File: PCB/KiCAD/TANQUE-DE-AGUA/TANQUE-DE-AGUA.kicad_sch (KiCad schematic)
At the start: 39 parts, among them J2 Vca_OUT, J5 HX30002-BA, Q1 2N3904, SW1 Nivel MAX, SW2 Nivel Min, U1 74HC00, U2 ULN2003, U3 LM7805, U4 74HC14, U5 MOC3021M, U6 BTA16-600C

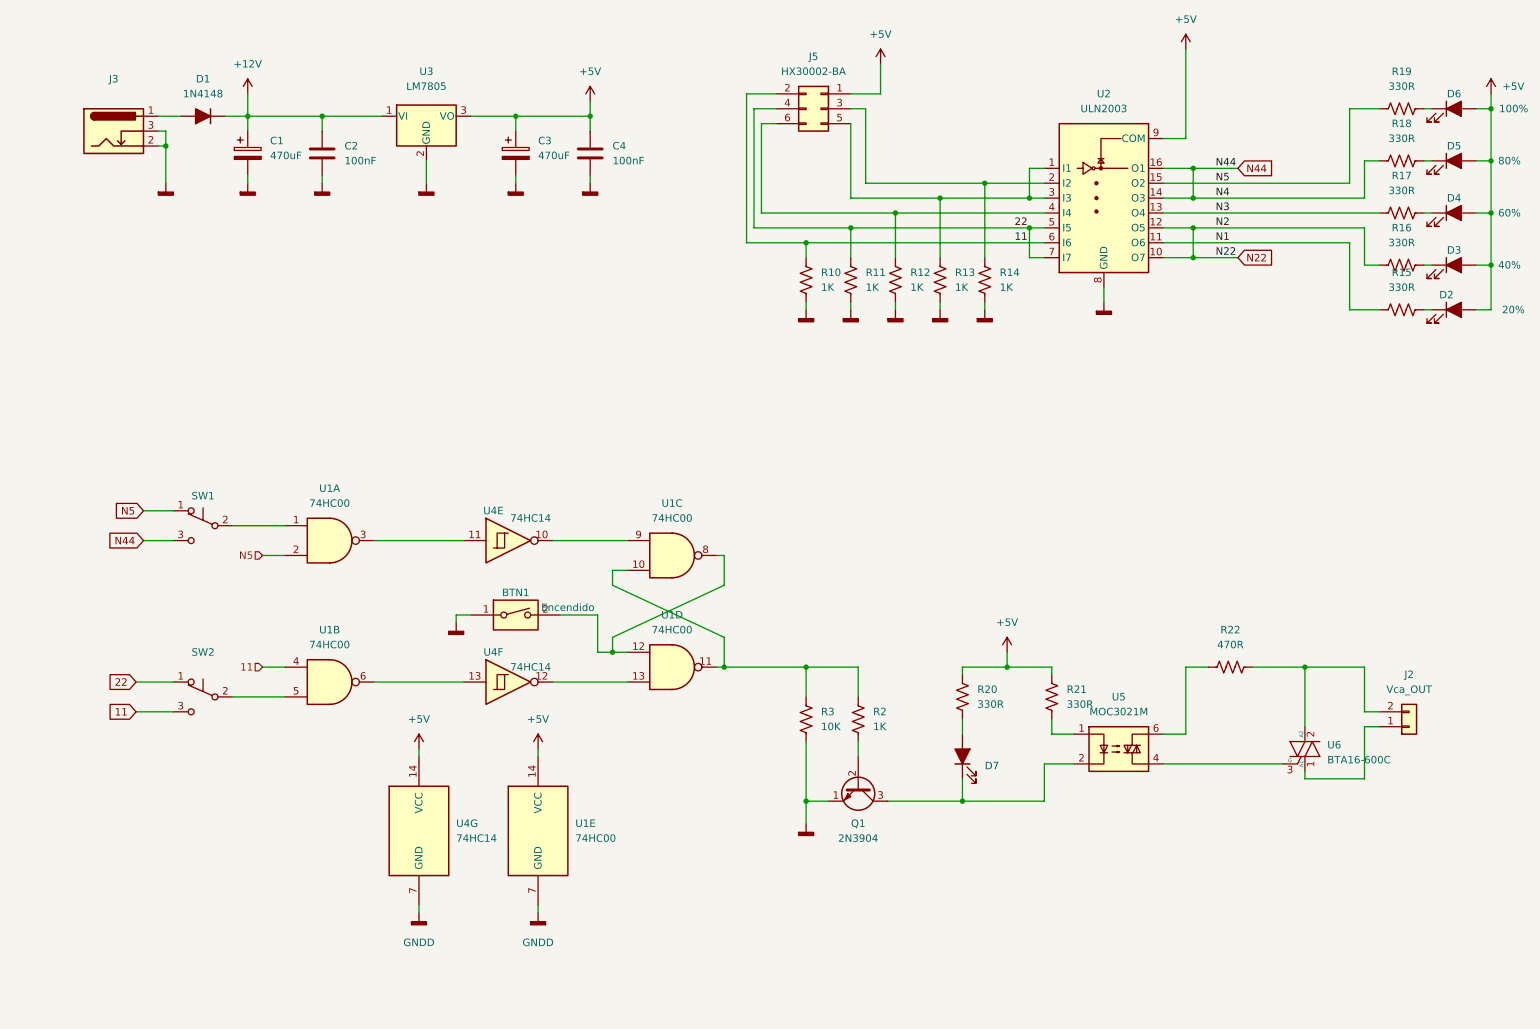
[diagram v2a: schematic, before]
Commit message: actualizacion del esquematico en Proteus y en KiCAD
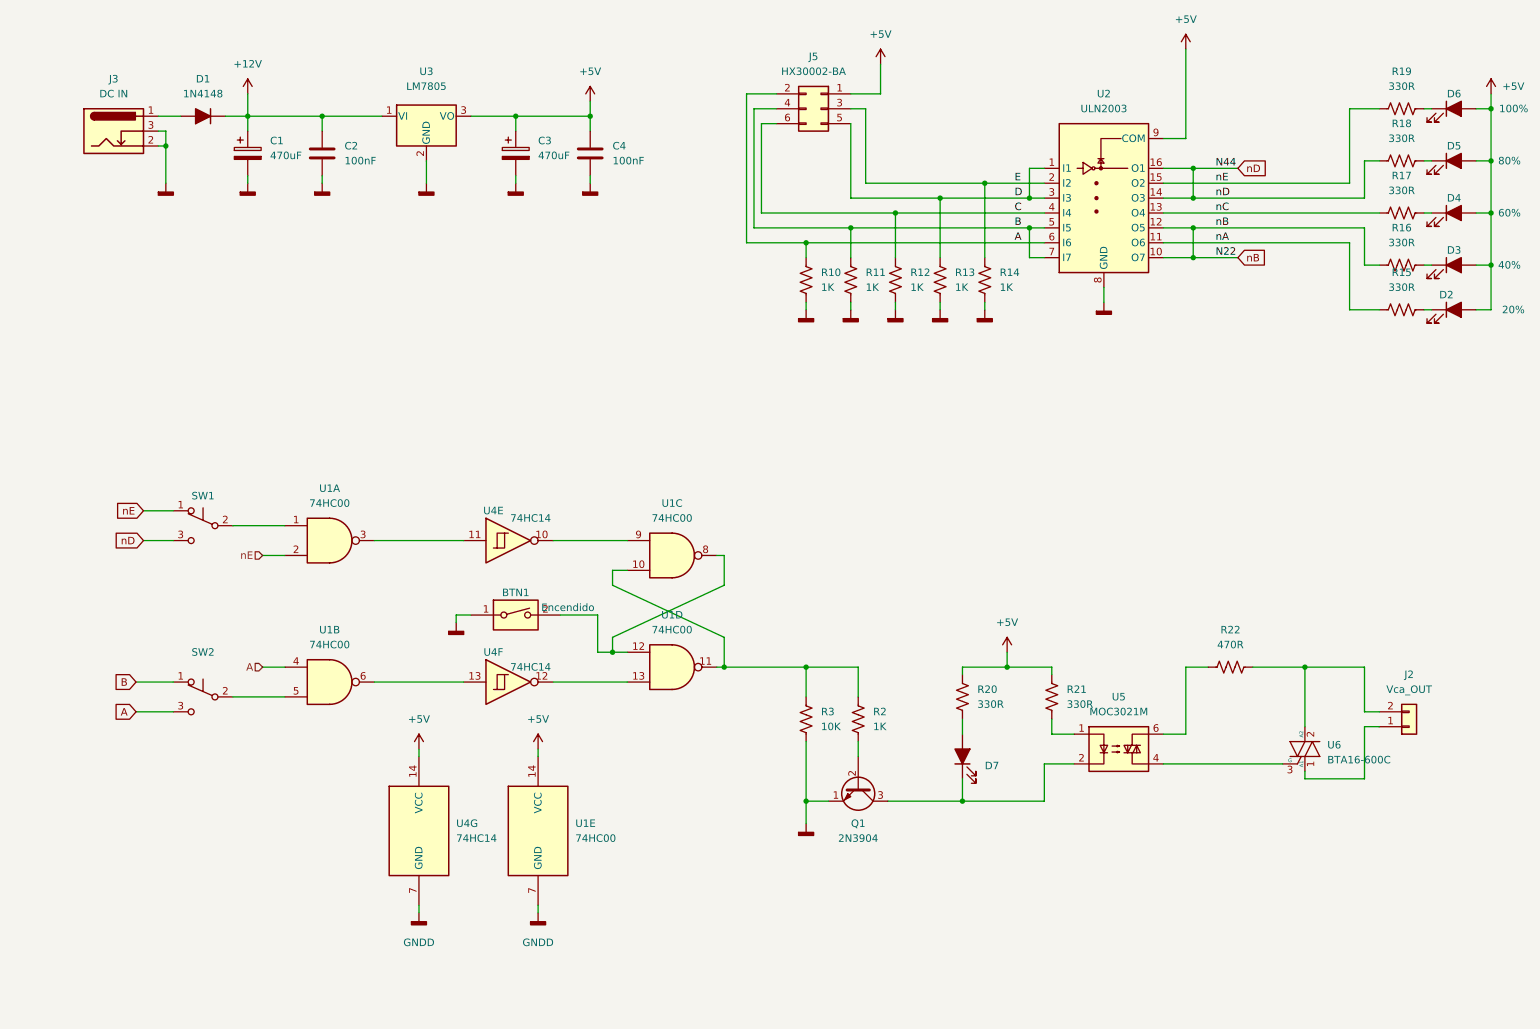
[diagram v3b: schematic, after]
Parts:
- J3: value (none) -> DC IN; footprint (none) -> Connector_BarrelJack:BarrelJack_Horizontal
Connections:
- net C: now reaches J5.6 (Pin_6), R12.1, U2.4 (I4)
- net E: now reaches J5.3 (Pin_3), R14.1, U2.2 (I2)
- net D: now reaches J5.5 (Pin_5), R13.1, U2.1 (I1), U2.3 (I3)
- net 11 renamed A
- net 22 renamed B
- net N1 renamed nA
- net N22 renamed nB
- net N3 renamed nC
- net N44 renamed nD
- net N5 renamed nE
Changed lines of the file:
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@@
     (stroke (width 0) (type default) (color 0 0 0 0))
   )
-  (label "N3" (at 220.98 50.8 0)
-    (effects (font (size 1.27 1.27)) (justify left bottom))
-  )
-  (label "N4" (at 220.98 48.26 0)
-    (effects (font (size 1.27 1.27)) (justify left bottom))
-  )
-  (label "N2" (at 220.98 53.34 0)
-    (effects (font (size 1.27 1.27)) (justify left bottom))
-  )
-  (label "N1" (at 220.98 55.88 0)
-    (effects (font (size 1.27 1.27)) (justify left bottom))
-  )
-  (label "N5" (at 220.98 45.72 0)
-    (effects (font (size 1.27 1.27)) (justify left bottom))
-  )
-  (label "11" (at 186.69 55.88 0)
+  (label "E" (at 186.69 45.72 0)
+    (effects (font (size 1.27 1.27)) (justify left bottom))
+  )
+  (label "nC" (at 220.98 50.8 0)
+    (effects (font (size 1.27 1.27)) (justify left bottom))
+  )
+  (label "nD" (at 220.98 48.26 0)
+    (effects (font (size 1.27 1.27)) (justify left bottom))
+  )
+  (label "nB" (at 220.98 53.34 0)
+    (effects (font (size 1.27 1.27)) (justify left bottom))
+  )
+  (label "D" (at 186.69 48.26 0)
+    (effects (font (size 1.27 1.27)) (justify left bottom))
+  )
+  (label "nA" (at 220.98 55.88 0)
+    (effects (font (size 1.27 1.27)) (justify left bottom))
+  )
+  (label "nE" (at 220.98 45.72 0)
+    (effects (font (size 1.27 1.27)) (justify left bottom))
+  )
+  (label "A" (at 186.69 55.88 0)
+    (effects (font (size 1.27 1.27)) (justify left bottom))
+  )
+  (label "C" (at 186.69 50.8 0)
     (effects (font (size 1.27 1.27)) (justify left bottom))
   )
@@
     (effects (font (size 1.27 1.27)) (justify left bottom))
   )
-  (label "22" (at 186.69 53.34 0)
-    (effects (font (size 1.27 1.27)) (justify left bottom))
-  )
-  (global_label "N22" (shape input) (at 224.79 58.42 0) (fields_autoplaced)
+  (label "B" (at 186.69 53.34 0)
+    (effects (font (size 1.27 1.27)) (justify left bottom))
+  )
+  (global_label "nB" (shape input) (at 224.79 58.42 0) (fields_autoplaced)
     (effects (font (size 1.27 1.27)) (justify left))
-    (property "Referencias entre hojas" "${INTERSHEET_REFS}" (id 0) (at 230.9526 58.3406 0)
+    (property "Referencias entre hojas" "${INTERSHEET_REFS}" (id 0) (at 229.6221 58.3406 0)
       (effects (font (size 1.27 1.27)) (justify left) hide)
     )
   )
-  (global_label "N44" (shape input) (at 38.1 106.68 180) (fields_autoplaced)
+  (global_label "nD" (shape input) (at 38.1 106.68 180) (fields_autoplaced)
     (effects (font (size 1.27 1.27)) (justify right))
-    (property "Referencias entre hojas" "${INTERSHEET_REFS}" (id 0) (at 31.9374 106.6006 0)
+    (property "Referencias entre hojas" "${INTERSHEET_REFS}" (id 0) (at 33.2679 106.6006 0)
       (effects (font (size 1.27 1.27)) (justify right) hide)
     )
   )
-  (global_label "N44" (shape input) (at 224.79 43.18 0) (fields_autoplaced)
+  (global_label "nD" (shape input) (at 224.79 43.18 0) (fields_autoplaced)
     (effects (font (size 1.27 1.27)) (justify left))
-    (property "Referencias entre hojas" "${INTERSHEET_REFS}" (id 0) (at 230.9526 43.1006 0)
+    (property "Referencias entre hojas" "${INTERSHEET_REFS}" (id 0) (at 229.6221 43.1006 0)
       (effects (font (size 1.27 1.27)) (justify left) hide)
     )
   )
-  (global_label "N5" (shape input) (at 38.1 101.6 180) (fields_autoplaced)
+  (global_label "nE" (shape input) (at 38.1 101.6 180) (fields_autoplaced)
     (effects (font (size 1.27 1.27)) (justify right))
-    (property "Referencias entre hojas" "${INTERSHEET_REFS}" (id 0) (at 33.1469 101.5206 0)
+    (property "Referencias entre hojas" "${INTERSHEET_REFS}" (id 0) (at 33.3888 101.5206 0)
       (effects (font (size 1.27 1.27)) (justify right) hide)
     )
   )
-  (global_label "22" (shape input) (at 36.83 130.81 180) (fields_autoplaced)
+  (global_label "B" (shape input) (at 36.83 130.81 180) (fields_autoplaced)
     (effects (font (size 1.27 1.27)) (justify right))
-    (property "Referencias entre hojas" "${INTERSHEET_REFS}" (id 0) (at 31.9979 130.7306 0)
+    (property "Referencias entre hojas" "${INTERSHEET_REFS}" (id 0) (at 33.1469 130.7306 0)
       (effects (font (size 1.27 1.27)) (justify right) hide)
     )
   )
-  (global_label "11" (shape input) (at 36.83 135.89 180) (fields_autoplaced)
+  (global_label "A" (shape input) (at 36.83 135.89 180) (fields_autoplaced)
     (effects (font (size 1.27 1.27)) (justify right))
-    (property "Referencias entre hojas" "${INTERSHEET_REFS}" (id 0) (at 31.9979 135.8106 0)
+    (property "Referencias entre hojas" "${INTERSHEET_REFS}" (id 0) (at 33.3283 135.8106 0)
       (effects (font (size 1.27 1.27)) (justify right) hide)
     )
   )
-  (hierarchical_label "11" (shape input) (at 58.42 128.27 180)
+  (hierarchical_label "A" (shape input) (at 58.42 128.27 180)
     (effects (font (size 1.27 1.27)) (justify right))
   )
-  (hierarchical_label "N5" (shape input) (at 58.42 109.22 180)
+  (hierarchical_label "nE" (shape input) (at 58.42 109.22 180)
     (effects (font (size 1.27 1.27)) (justify right))
   )
@@
     (in_bom yes) (on_board yes) (fields_autoplaced)
     (property "Reference" "J3" (id 0) (at 33.02 27.94 0))
-    (property "Value" "" (id 1) (at 33.02 30.48 0))
-    (property "Footprint" "" (id 2) (at 34.29 37.846 0)
-      (effects (font (size 1.27 1.27)) hide)
-    )
+    (property "Value" "DC IN" (id 1) (at 33.02 30.48 0))
+    (property "Footprint" "Connector_BarrelJack:BarrelJack_Horizontal" (id 2) (at 34.29 37.846 0)
+      (effects (font (size 1.27 1.27)) hide)
+    )

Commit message: actualizacion del PCB
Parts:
- added H1, H2, H3, H4: MountingHole, MountingHole:MountingHole_2.7mm_M2.5, symbol Mechanical:MountingHole
- C1, C3: footprint Capacitor_THT:CP_Radial_D6.3mm_P2.50mm -> (none)
- Q1: footprint Package_TO_SOT_THT:TO-92_Inline -> Package_TO_SOT_THT:TO-92_Wide
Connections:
- net nE: now also U1.1; no longer U1.2
- net at SW1.2 (B): now also U1.2; no longer U1.1
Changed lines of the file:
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@@
     (pin "2")
   )
-  (symbol (lib_id "74xx:74HC00") (at 69.85 106.68 0) (unit 1)
+  (symbol (lib_id "74xx:74HC00") (at 69.85 106.68 0) (mirror x) (unit 1)
     (in_bom yes) (on_board yes) (fields_autoplaced)
     (property "Reference" "U1" (id 0) (at 69.85 97.79 0))
@@
       (effects (font (size 1.27 1.27)) (justify left))
     )
-    (property "Footprint" "Capacitor_THT:CP_Radial_D6.3mm_P2.50mm" (id 2) (at 102.5652 44.45 0)
+    (property "Footprint" "" (id 2) (at 102.5652 44.45 0)
       (effects (font (size 1.27 1.27)) hide)
     )
@@
     (property "Reference" "Q1" (id 0) (at 160.02 154.94 90))
     (property "Value" "2N3904" (id 1) (at 160.02 157.48 90))
-    (property "Footprint" "Package_TO_SOT_THT:TO-92_Inline" (id 2) (at 158.115 153.67 0)
+    (property "Footprint" "Package_TO_SOT_THT:TO-92_Wide" (id 2) (at 158.115 153.67 0)
       (effects (font (size 1.27 1.27) italic) (justify left) hide)
     )
@@
     (pin "3")
   )
+  (symbol (lib_id "Mechanical:MountingHole") (at 247.65 88.9 0) (unit 1)
+    (in_bom yes) (on_board yes) (fields_autoplaced)
+    (property "Reference" "H1" (id 0) (at 250.19 87.6299 0)
+      (effects (font (size 1.27 1.27)) (justify left) hide)
+    )
+    (property "Value" "MountingHole" (id 1) (at 250.19 88.8999 0)
+      (effects (font (size 1.27 1.27)) (justify left) hide)
+    )
+    (property "Footprint" "MountingHole:MountingHole_2.7mm_M2.5" (id 2) (at 247.65 88.9 0)
+      (effects (font (size 1.27 1.27)) hide)
+    )
+    (property "Datasheet" "~" (id 3) (at 247.65 88.9 0)
+      (effects (font (size 1.27 1.27)) hide)
+    )
+  )
   (symbol (lib_id "Device:C_Polarized") (at 55.88 40.64 0) (unit 1)
     (in_bom yes) (on_board yes) (fields_autoplaced)
@@
       (effects (font (size 1.27 1.27)) (justify left))
     )
-    (property "Footprint" "Capacitor_THT:CP_Radial_D6.3mm_P2.50mm" (id 2) (at 56.8452 44.45 0)
+    (property "Footprint" "" (id 2) (at 56.8452 44.45 0)
       (effects (font (size 1.27 1.27)) hide)
     )
@@
     (pin "1")
     (pin "2")
+  )
+  (symbol (lib_id "Mechanical:MountingHole") (at 247.65 115.57 0) (unit 1)
+    (in_bom yes) (on_board yes) (fields_autoplaced)
+    (property "Reference" "H4" (id 0) (at 250.19 114.2999 0)
+      (effects (font (size 1.27 1.27)) (justify left) hide)
+    )
+    (property "Value" "MountingHole" (id 1) (at 250.19 116.8399 0)
+      (effects (font (size 1.27 1.27)) (justify left) hide)
+    )
+    (property "Footprint" "MountingHole:MountingHole_2.7mm_M2.5" (id 2) (at 247.65 115.57 0)
+      (effects (font (size 1.27 1.27)) hide)
+    )
+    (property "Datasheet" "~" (id 3) (at 247.65 115.57 0)
+      (effects (font (size 1.27 1.27)) hide)
+    )
   )
   (symbol (lib_id "power:GNDD") (at 55.88 45.72 0) (unit 1)
@@
     (pin "2")
   )
+  (symbol (lib_id "Mechanical:MountingHole") (at 247.65 97.79 0) (unit 1)
+    (in_bom yes) (on_board yes) (fields_autoplaced)
+    (property "Reference" "H2" (id 0) (at 250.19 96.5199 0)
+      (effects (font (size 1.27 1.27)) (justify left) hide)
+    )
+    (property "Value" "MountingHole" (id 1) (at 250.19 99.0599 0)
+      (effects (font (size 1.27 1.27)) (justify left) hide)
+    )
+    (property "Footprint" "MountingHole:MountingHole_2.7mm_M2.5" (id 2) (at 247.65 97.79 0)
+      (effects (font (size 1.27 1.27)) hide)
+    )
+    (property "Datasheet" "~" (id 3) (at 247.65 97.79 0)
+      (effects (font (size 1.27 1.27)) hide)
+    )
+  )
   (symbol (lib_id "power:+12V") (at 55.88 30.48 0) (unit 1)
     (in_bom yes) (on_board yes) (fields_autoplaced)
@@
     )
     (pin "1")
+  )
+  (symbol (lib_id "Mechanical:MountingHole") (at 247.65 106.68 0) (unit 1)
+    (in_bom yes) (on_board yes) (fields_autoplaced)
+    (property "Reference" "H3" (id 0) (at 250.19 105.4099 0)
+      (effects (font (size 1.27 1.27)) (justify left) hide)
+    )
+    (property "Value" "MountingHole" (id 1) (at 250.19 107.9499 0)
+      (effects (font (size 1.27 1.27)) (justify left) hide)
+    )
+    (property "Footprint" "MountingHole:MountingHole_2.7mm_M2.5" (id 2) (at 247.65 106.68 0)
+      (effects (font (size 1.27 1.27)) hide)
+    )
+    (property "Datasheet" "~" (id 3) (at 247.65 106.68 0)
+      (effects (font (size 1.27 1.27)) hide)
+    )
   )
   (symbol (lib_id "74xx:74HC00") (at 105.41 156.21 0) (unit 5)
@@
     )
     (path "/9498f042-02bb-40fc-9ba4-8649cd18fbfe"
-      (reference "C1") (unit 1) (value "470uF") (footprint "Capacitor_THT:CP_Radial_D6.3mm_P2.50mm")
+      (reference "C1") (unit 1) (value "470uF") (footprint "Capacitor_THT:CP_Radial_D8.0mm_P3.50mm")
     )
     (path "/4c12bbfb-29b8-49c1-be43-6ec6461cd547"
@@
     )
     (path "/7838ec13-a1dc-4ebb-8a90-aada206acddb"
-      (reference "C3") (unit 1) (value "470uF") (footprint "Capacitor_THT:CP_Radial_D6.3mm_P2.50mm")
+      (reference "C3") (unit 1) (value "470uF") (footprint "Capacitor_THT:CP_Radial_D8.0mm_P3.50mm")
     )
     (path "/32b9fb0b-5d7d-4fac-93ef-206883ef1965"
@@
       (reference "D7") (unit 1) (value "ENCENDIDO") (footprint "LED_THT:LED_D3.0mm_IRGrey")
     )
+    (path "/942b3d2a-6e53-4478-a7d2-e49c39cd043d"
+      (reference "H1") (unit 1) (value "MountingHole") (footprint "MountingHole:MountingHole_2.7mm_M2.5")
+    )
+    (path "/b158a7ba-bb21-4131-9851-8f8f201bd693"
+      (reference "H2") (unit 1) (value "MountingHole") (footprint "MountingHole:MountingHole_2.7mm_M2.5")
+    )
+    (path "/c3859b88-ee1c-4daa-9fe4-63386a16086c"
+      (reference "H3") (unit 1) (value "MountingHole") (footprint "MountingHole:MountingHole_2.7mm_M2.5")
+    )
+    (path "/9bdeda29-d138-4c87-b429-3ac24826c6e2"
+      (reference "H4") (unit 1) (value "MountingHole") (footprint "MountingHole:MountingHole_2.7mm_M2.5")
+    )
     (path "/b0bf8413-8ba5-4e4d-a530-2221d2c18f5a"
       (reference "J2") (unit 1) (value "Vca_OUT") (footprint "TerminalBlock_Phoenix:TerminalBlock_Phoenix_MPT-0,5-2-2.54_1x02_P2.54mm_Horizontal")
@@
     )
     (path "/925725a4-34ed-4683-b608-5db3c4c75819"
-      (reference "Q1") (unit 1) (value "2N3904") (footprint "Package_TO_SOT_THT:TO-92_Inline")
+      (reference "Q1") (unit 1) (value "2N3904") (footprint "Package_TO_SOT_THT:TO-92_Wide")
     )
     (path "/617c7f85-24d1-42e2-8f03-8f50f89ea4ba"
